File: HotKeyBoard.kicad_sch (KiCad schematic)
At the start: 150 parts, among them J1 Conn_01x12_Socket, J2 Conn_01x12_Socket, SW1 SW_Push, SW10 SW_Push, SW11 SW_Push, SW12 SW_Push, SW13 SW_Push, SW14 SW_Push, SW15 SW_Push, SW16 SW_Push, SW17 SW_Push, SW18 SW_Push, SW19 SW_Push, SW2 SW_Push, SW20 SW_Push, SW21 SW_Push, SW22 SW_Push, SW23 SW_Push, SW24 SW_Push, SW25 SW_Push, SW26 SW_Push, SW27 SW_Push, SW28 SW_Push, SW29 SW_Push, SW3 SW_Push, SW30 SW_Push, SW31 SW_Push, SW32 SW_Push, SW33 SW_Push, SW34 SW_Push, SW35 SW_Push, SW36 SW_Push, SW37 SW_Push, SW38 SW_Push, SW39 SW_Push, SW4 SW_Push, SW40 SW_Push, SW41 SW_Push, SW42 SW_Push, SW43 SW_Push, SW44 SW_Push, SW45 SW_Push, SW46 SW_Push, SW47 SW_Push, SW48 SW_Push, SW49 SW_Push, SW5 SW_Push, SW50 SW_Push, SW51 SW_Push, SW52 SW_Push, SW53 SW_Push, SW54 SW_Push, SW55 SW_Push, SW56 SW_Push, SW57 SW_Push, SW58 SW_Push, SW59 SW_Push, SW6 SW_Push, SW60 SW_Push, SW61 SW_Push, SW62 SW_Push, SW63 SW_Push, SW64 SW_Push, SW65 SW_Push, SW66 SW_Push, SW67 SW_Push, SW68 SW_Push, SW69 SW_Push, SW7 SW_Push, SW70 SW_Push, SW71 SW_Push, SW72 SW_Push, SW8 SW_Push, SW9 SW_Push

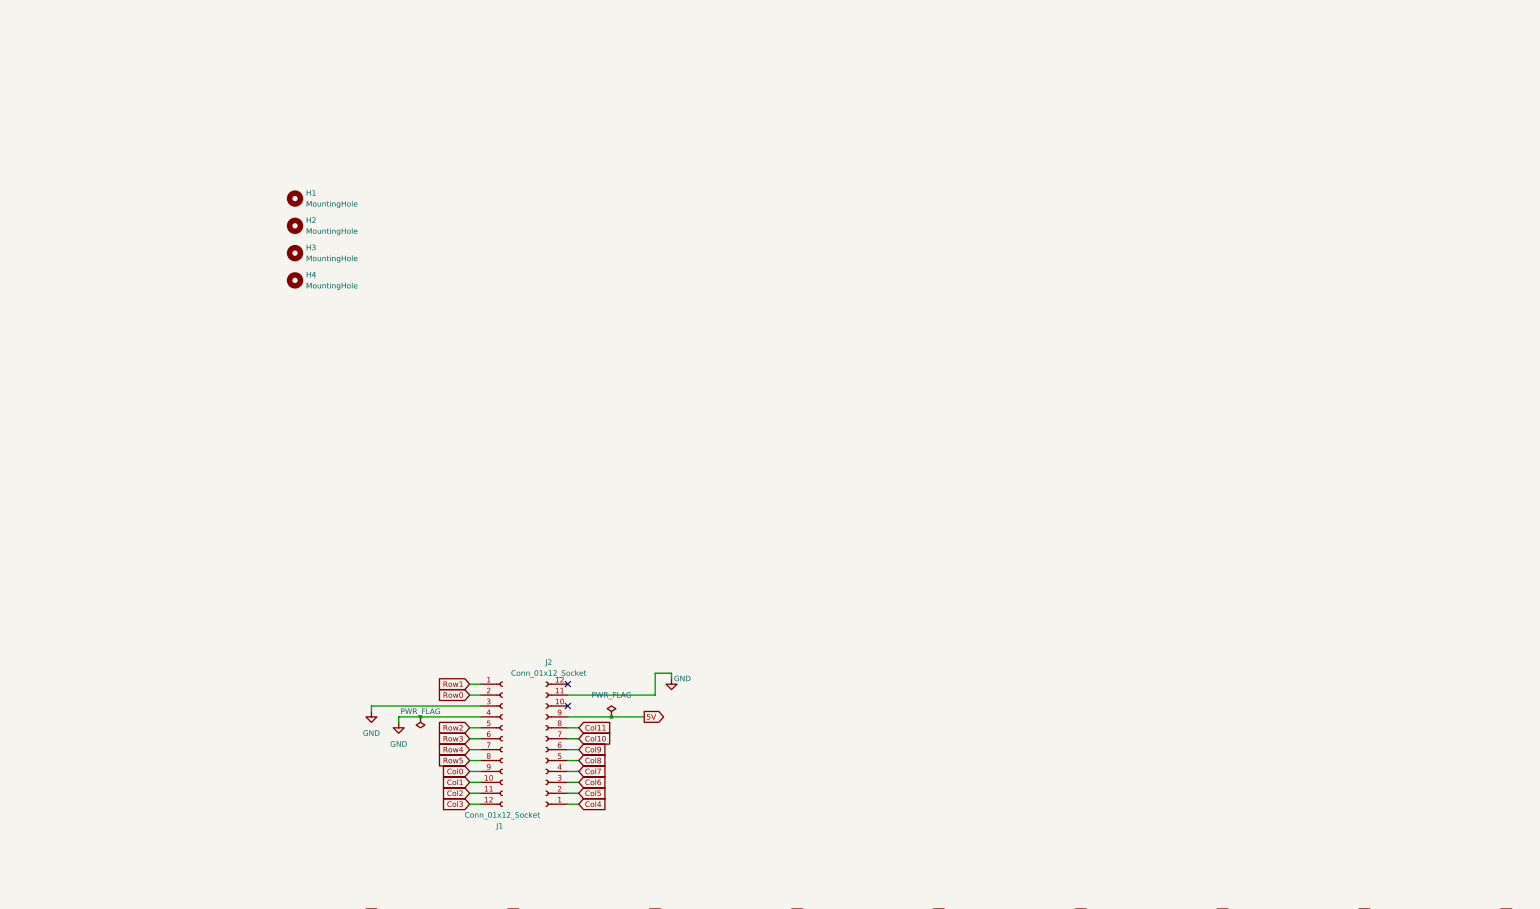
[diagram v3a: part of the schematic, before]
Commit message: Started doing the schematic
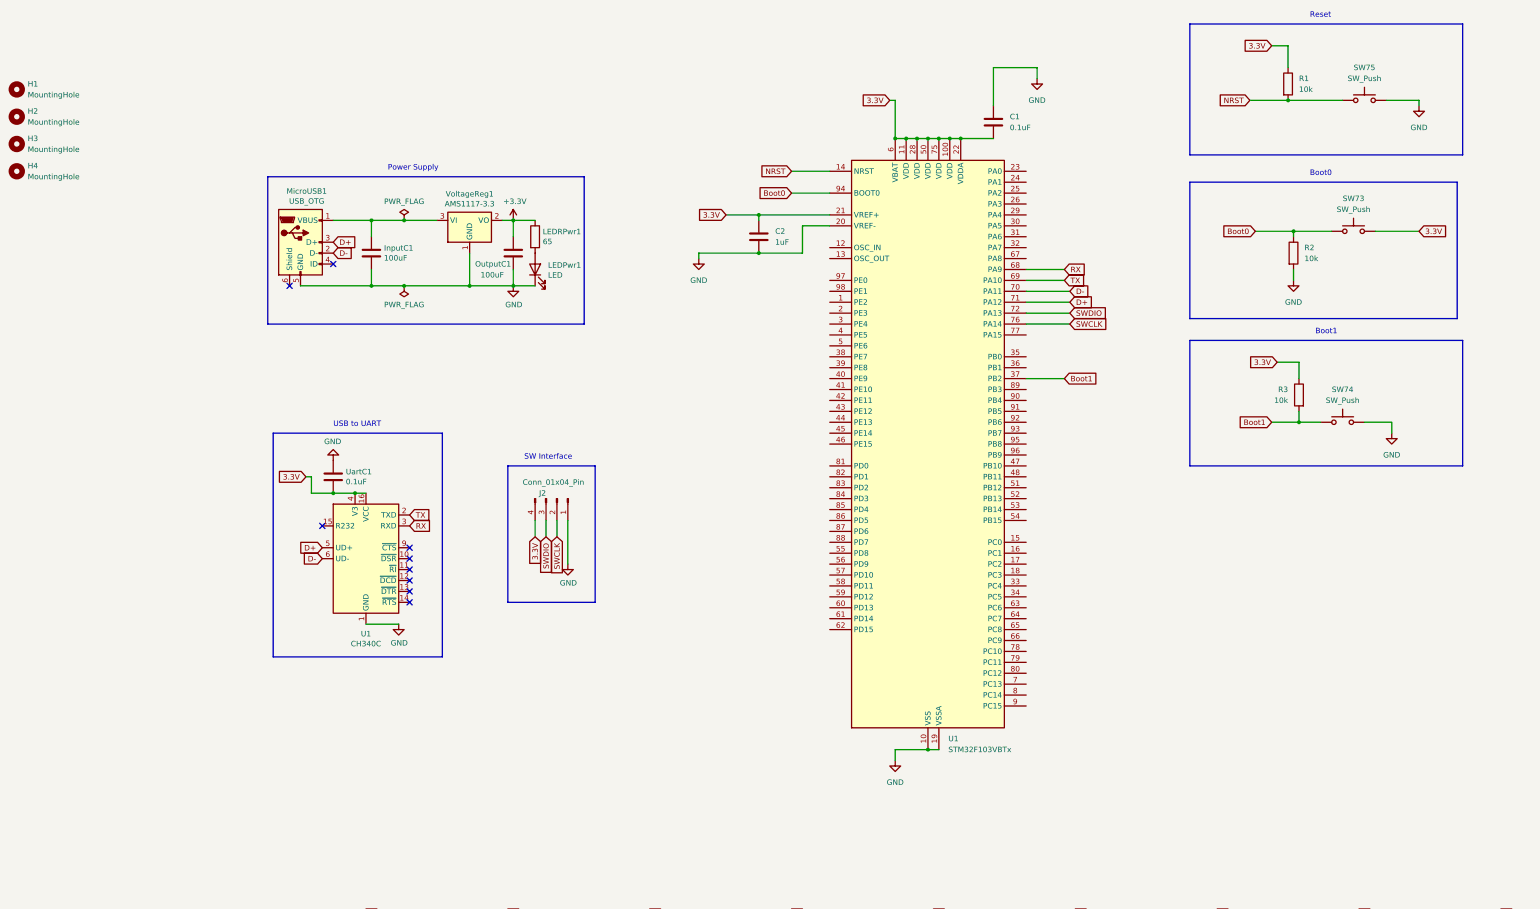
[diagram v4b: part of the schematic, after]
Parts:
- removed J1, J2: Conn_01x12_Socket, Connector_PinHeader_2.54mm:PinHeader_1x12_P2.54mm_Vertical, symbol Connector:Conn_01x12_Socket
- added C1: 0.1uF, symbol Device:C
- added C2: 1uF, symbol Device:C
- added InputC1, OutputC1: 100uF, Capacitor_THT:C_Radial_D5.0mm_H7.0mm_P2.00mm, symbol Device:C
- added J2: Conn_01x04_Pin, symbol Connector:Conn_01x04_Pin
- added LEDPwr1: LED, LED_SMD:LED_0402_1005Metric, symbol Device:LED
- added LEDRPwr1: 65, Resistor_THT:R_Axial_DIN0207_L6.3mm_D2.5mm_P7.62mm_Horizontal, symbol Device:R
- added MicroUSB1: USB_OTG, Connector_USB:USB_Micro-B_Molex_47346-0001, symbol Connector:USB_OTG
- added R1, R2, R3: 10k, symbol Device:R
- added SW73, SW74, SW75: SW_Push, symbol Switch:SW_Push
- added U1: CH340C, Package_SO:SOIC-16_3.9x9.9mm_P1.27mm, symbol Interface_USB:CH340C
- added U1: STM32F103VBTx, Package_QFP:LQFP-100_14x14mm_P0.5mm, symbol MCU_ST_STM32F1:STM32F103VBTx
- added UartC1: 0.1uF, Capacitor_THT:C_Radial_D5.0mm_H7.0mm_P2.00mm, symbol Device:C
- added VoltageReg1: AMS1117-3.3, Package_TO_SOT_SMD:SOT-223-3_TabPin2, symbol Regulator_Linear:AMS1117-3.3
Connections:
- net GND: now also C1.1, C2.2, InputC1.2, J2.1 (Pin_1), LEDPwr1.1 (K), MicroUSB1.5 (GND), OutputC1.2, R2.2, SW74.2, SW75.2, U1.1 (GND), U1.10 (VSS), U1.19 (VSSA), U1.20 (VREF-), U1.27 (VSS), U1.49 (VSS), U1.74 (VSS), U1.99 (VSS), UartC1.1, VoltageReg1.1 (GND)
- new net: LEDPwr1.2 (A), LEDRPwr1.2
- new net: InputC1.1, MicroUSB1.1 (VBUS), VoltageReg1.3 (VI)
- new net +3V3: LEDRPwr1.1, OutputC1.1, VoltageReg1.2 (VO)
- new net 3.3V: C1.2, C2.1, J2.4 (Pin_4), R1.1, R3.1, SW73.2, U1.100 (VDD), U1.11 (VDD), U1.16 (VCC), U1.21 (VREF+), U1.22 (VDDA), U1.28 (VDD), U1.4 (V3), U1.50 (VDD), U1.6 (VBAT), U1.75 (VDD), UartC1.2
- new net Boot0: R2.1, SW73.1, U1.94 (BOOT0)
- new net Boot1: R3.2, SW74.1, U1.37 (PB2)
- new net D+: MicroUSB1.3 (D+), U1.5 (UD+), U1.71 (PA12)
- new net D-: MicroUSB1.2 (D-), U1.6 (UD-), U1.70 (PA11)
- new net NRST: R1.2, SW75.1, U1.14 (NRST)
- new net RX: U1.3 (RXD), U1.68 (PA9)
- new net SWCLK: J2.2 (Pin_2), U1.76 (PA14)
- new net SWDIO: J2.3 (Pin_3), U1.72 (PA13)
- new net TX: U1.2 (TXD), U1.69 (PA10)
- no-connect marks 2 -> 9
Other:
- note added: "Boot0"
- note added: "Boot1"
- note added: "Power Supply"
- note added: "Reset"
- note added: "SW Interface"
- note added: "USB to UART"
- moved on the sheet: H1, H2, H3, H4

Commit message: Finished schematic
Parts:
- added D100, D101, D102, D103, D104, D105, D106, D107, D108, D109, D110, D111, D112, D113, D114, D115, D116, D117, D118, D119, D120, D121, D122, D123, D124, D125, D126, D127, D128, D129, D130, D131, D132, D133, D134, D135, D136, D137, D138, D139, D140, D141, D142, D143, D144, D145, D146, D147, D148, D149, D150, D151, D152, D153, D154, D155, D156, D157, D158, D159, D160, D161, D162, D163, D164, D165, D166, D167, D168, D169, D170, D171, D172, D173, D174, D175, D176, D177, D178, D179, D180, D181, D182, D183, D184, D185, D186, D187, D188, D189, D190, D191, D192, D97, D98, D99: LED, LED_SMD:LED_0402_1005Metric, symbol Device:LED
- added D73, D74, D75, D76, D77, D78, D79, D80, D81, D82, D83, D84, D85, D86, D87, D88, D89, D90, D91, D92, D93, D94, D95, D96: D, Diode_SMD:D_SOD-323, symbol Device:D
- added J1: Conn_01x04_Pin, Connector_PinHeader_2.54mm:PinHeader_1x04_P2.54mm_Vertical, symbol Connector:Conn_01x04_Pin
- added J3: USB_VOLTAGE Measuring Point, Connector_PinHeader_2.54mm:PinHeader_1x01_P2.54mm_Vertical, symbol Connector:Conn_01x01_Pin
- added J4: LED_VOLTAGE Measuring Point 1, Connector_PinHeader_2.54mm:PinHeader_1x01_P2.54mm_Vertical, symbol Connector:Conn_01x01_Pin
- added J5: LED_VOLTAGE Measuring Point 2, Connector_PinHeader_2.54mm:PinHeader_1x01_P2.54mm_Vertical, symbol Connector:Conn_01x01_Pin
- added Q1, Q2, Q3, Q4, Q5, Q6: IRLZ34N, Package_TO_SOT_THT:TO-220-3_Vertical, symbol Transistor_FET:IRLZ34N
- added R10, R11, R12, R13, R14, R15, R16, R17, R18, R19, R20, R21, R22, R23, R24, R25, R26, R27, R28, R29, R30, R31, R32, R33, R34, R35, R36, R37, R38, R39, R4, R40, R41, R42, R43, R44, R45, R46, R47, R48, R49, R5, R50, R51, R52, R53, R54, R55, R56, R57, R58, R59, R6, R60, R61, R62, R63, R64, R65, R66, R67, R68, R69, R7, R70, R71, R72, R73, R74, R75, R76, R77, R78, R79, R8, R80, R81, R82, R83, R84, R85, R86, R87, R88, R89, R9, R90, R91, R92, R93, R94, R95, R96, R97, R98, R99: R, Resistor_SMD:R_0603_1608Metric, symbol Device:R
- added SW76, SW77, SW78, SW80, SW81, SW82, SW83, SW84, SW86, SW87, SW88, SW89, SW90, SW92, SW93, SW94, SW95, SW96, SW98, SW99: SW_Push, Button_Switch_Keyboard:SW_Cherry_MX_1.00u_PCB, symbol Switch:SW_Push
- added SW79, SW85, SW91, SW97: SW_Push, Button_Switch_Keyboard:SW_Cherry_MX_1.75u_PCB, symbol Switch:SW_Push
- added U2, U4: AMS1117-3.3, Package_TO_SOT_SMD:SOT-223-3_TabPin2, symbol Regulator_Linear:AMS1117-3.3
- C1: footprint (none) -> Capacitor_SMD:C_0402_1005Metric; LCSC (none) -> C307331
- C2: footprint (none) -> Capacitor_SMD:C_0603_1608Metric; LCSC (none) -> C15849
- InputC1, OutputC1: footprint Capacitor_THT:C_Radial_D5.0mm_H7.0mm_P2.00mm -> Capacitor_SMD:C_1206_3216Metric; LCSC (none) -> C15008
- J2: footprint (none) -> Connector_PinHeader_2.54mm:PinHeader_1x04_P2.54mm_Vertical
- LEDPwr1: LCSC (none) -> C71911
- LEDRPwr1: LCSC (none) -> C307279
- R1, R2, R3: footprint (none) -> Resistor_SMD:R_0603_1608Metric; LCSC (none) -> C25804
- SW73, SW74, SW75: footprint (none) -> Button_Switch_Keyboard:SW_Cherry_MX_1.00u_PCB
- U1: LCSC (none) -> C84681
- UartC1: footprint Capacitor_THT:C_Radial_D5.0mm_H7.0mm_P2.00mm -> Capacitor_SMD:C_0402_1005Metric; LCSC (none) -> C307331
- VoltageReg1: LCSC (none) -> C347256
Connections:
- net +3V3 is gone; now on net 3.3V: LEDRPwr1.1, OutputC1.1, VoltageReg1.2 (VO)
- net 3.3V: now also J1.4 (Pin_4)
- net Col0: now also U1.81 (PD0)
- net Col1: now also U1.82 (PD1)
- net Col10: now also U1.57 (PD10)
- net Col11: now also U1.58 (PD11)
- net Col2: now also U1.83 (PD2)
- net Col3: now also U1.84 (PD3)
- net Col4: now also U1.85 (PD4)
- net Col5: now also U1.86 (PD5)
- net Col6: now also U1.87 (PD6)
- net Col7: now also U1.88 (PD7)
- net Col8: now also U1.55 (PD8)
- net Col9: now also U1.56 (PD9)
- net GND: now also J1.3 (Pin_3), Q1.3 (S), Q2.3 (S), Q3.3 (S), Q4.3 (S), Q5.3 (S), Q6.3 (S), U2.1 (GND), U4.1 (GND)
- net Row0: now also U1.97 (PE0), D73.1 (K), D79.1 (K), D85.1 (K), D91.1 (K)
- net Row1: now also U1.98 (PE1), D74.1 (K), D80.1 (K), D86.1 (K), D92.1 (K)
- net Row2: now also U1.1 (PE2), D75.1 (K), D81.1 (K), D87.1 (K), D93.1 (K)
- net Row3: now also U1.2 (PE3), D76.1 (K), D82.1 (K), D88.1 (K), D94.1 (K)
- net Row4: now also U1.3 (PE4), D77.1 (K), D83.1 (K), D89.1 (K), D95.1 (K)
- net Row5: now also U1.4 (PE5), D78.1 (K), D84.1 (K), D90.1 (K), D96.1 (K)
- net USB_VOLT: now reaches InputC1.1, MicroUSB1.1 (VBUS), VoltageReg1.3 (VI)
- net USB_VOLT: now also J3.1 (Pin_1), U2.3 (VI), U4.3 (VI)
- net Row7: now reaches U1.38 (PE7)
- net Row8: now reaches U1.39 (PE8)
- net Row9: now reaches U1.40 (PE9)
- net Row10: now reaches U1.41 (PE10)
- net Row11: now reaches U1.42 (PE11)
- net Row12: now reaches U1.43 (PE12)
- net Row13: now reaches U1.44 (PE13)
- net Row14: now reaches U1.45 (PE14)
- net Row15: now reaches U1.46 (PE15)
- net I2C_SCL: now reaches U1.47 (PB10)
- net I2C_SCL: now also J1.2 (Pin_2)
- net I2C_SDA: now reaches U1.48 (PB11)
- net I2C_SDA: now also J1.1 (Pin_1)
- net Row6: now reaches U1.5 (PE6)
- net Col12: now reaches U1.59 (PD12)
- net Col12: now also SW76.1, SW77.1, SW78.1, SW79.1, SW80.1, SW81.1
- net Col13: now reaches U1.60 (PD13)
- net Col13: now also SW82.1, SW83.1, SW84.1, SW85.1, SW86.1, SW87.1
- net Col14: now reaches U1.61 (PD14)
- net Col14: now also SW88.1, SW89.1, SW90.1, SW91.1, SW92.1, SW93.1
- net Col15: now reaches U1.62 (PD15)
- net Col15: now also SW94.1, SW95.1, SW96.1, SW97.1, SW98.1, SW99.1
- net Gate3: now reaches U1.63 (PC6)
- net Gate3: now also Q4.1 (G)
- net Gate4: now reaches U1.64 (PC7)
- net Gate4: now also Q5.1 (G)
- net Gate5: now reaches U1.65 (PC8)
- net Gate5: now also Q6.1 (G)
- net Gate0: now reaches U1.89 (PB3)
- net Gate0: now also Q1.1 (G)
- net Gate1: now reaches U1.90 (PB4)
- net Gate1: now also Q2.1 (G)
- net Gate2: now reaches U1.91 (PB5)
- net Gate2: now also Q3.1 (G)
- new net: D145.2 (A), R52.2
- new net: D186.2 (A), R93.2
- new net: D101.2 (A), R8.2
- new net: D85.2 (A), SW88.2
- new net: D86.2 (A), SW89.2
- new net: D137.2 (A), R44.2
- new net: D108.2 (A), R15.2
- new net: D183.2 (A), R90.2
- new net: D180.2 (A), R87.2
- new net: D128.2 (A), R35.2
- new net: D94.2 (A), SW97.2
- new net: D187.2 (A), R94.2
- new net: D170.2 (A), R77.2
- new net: D158.2 (A), R65.2
- new net: D107.2 (A), R14.2
- new net: D126.2 (A), R33.2
- new net: D160.2 (A), R67.2
- new net: D73.2 (A), SW76.2
- new net: D189.2 (A), R96.2
- new net: D165.2 (A), R72.2
- new net: D157.2 (A), R64.2
- new net: D115.2 (A), R22.2
- new net: D83.2 (A), SW86.2
- new net: D92.2 (A), SW95.2
- new net: D182.2 (A), R89.2
- new net: D106.2 (A), R13.2
- new net: D149.2 (A), R56.2
- new net: D184.2 (A), R91.2
- new net: D134.2 (A), R41.2
- new net: D143.2 (A), R50.2
- new net: D179.2 (A), R86.2
- new net: D111.2 (A), R18.2
- new net: D123.2 (A), R30.2
- new net: D129.2 (A), R36.2
- new net: D150.2 (A), R57.2
- new net: D113.2 (A), R20.2
- new net: D120.2 (A), R27.2
- new net: D118.2 (A), R25.2
- new net: D135.2 (A), R42.2
- new net: D77.2 (A), SW80.2
- new net: D140.2 (A), R47.2
- new net: D81.2 (A), SW84.2
- new net: D164.2 (A), R71.2
- new net: D174.2 (A), R81.2
- new net: D103.2 (A), R10.2
- new net: D130.2 (A), R37.2
- new net: D117.2 (A), R24.2
- new net: D192.2 (A), R99.2
- new net: D102.2 (A), R9.2
- new net: D80.2 (A), SW83.2
- new net: D138.2 (A), R45.2
- new net: D88.2 (A), SW91.2
- new net: D124.2 (A), R31.2
- new net: D104.2 (A), R11.2
- new net: D171.2 (A), R78.2
- new net: D141.2 (A), R48.2
- new net: D177.2 (A), R84.2
- new net: D121.2 (A), R28.2
- new net: D168.2 (A), R75.2
- new net: D125.2 (A), R32.2
- new net: D97.2 (A), R4.2
- new net: D105.2 (A), R12.2
- new net: D109.2 (A), R16.2
- new net: D176.2 (A), R83.2
- new net: D175.2 (A), R82.2
- new net: D156.2 (A), R63.2
- new net: D185.2 (A), R92.2
- new net: D169.2 (A), R76.2
- new net: D127.2 (A), R34.2
- new net: D91.2 (A), SW94.2
- new net: D100.2 (A), R7.2
- new net: D139.2 (A), R46.2
- new net: D74.2 (A), SW77.2
- new net: D131.2 (A), R38.2
- new net: D95.2 (A), SW98.2
- new net: D167.2 (A), R74.2
- new net: D112.2 (A), R19.2
- new net: D162.2 (A), R69.2
- new net: D122.2 (A), R29.2
- new net: D144.2 (A), R51.2
- new net: D142.2 (A), R49.2
- new net: D87.2 (A), SW90.2
- new net: D133.2 (A), R40.2
- new net: D76.2 (A), SW79.2
- new net: D93.2 (A), SW96.2
- new net: D173.2 (A), R80.2
- new net: D89.2 (A), SW92.2
- new net: D99.2 (A), R6.2
- new net: D132.2 (A), R39.2
- new net: D110.2 (A), R17.2
- new net: D159.2 (A), R66.2
- new net: D163.2 (A), R70.2
- new net: D191.2 (A), R98.2
- new net: D178.2 (A), R85.2
- new net: D190.2 (A), R97.2
- new net: D161.2 (A), R68.2
- new net: D136.2 (A), R43.2
- new net: D155.2 (A), R62.2
- new net: D148.2 (A), R55.2
- new net: D172.2 (A), R79.2
- new net: D79.2 (A), SW82.2
- new net: D147.2 (A), R54.2
- new net: D78.2 (A), SW81.2
- new net: D114.2 (A), R21.2
- new net: D75.2 (A), SW78.2
- new net: D153.2 (A), R60.2
- new net: D181.2 (A), R88.2
- new net: D152.2 (A), R59.2
- new net: D116.2 (A), R23.2
- new net: D96.2 (A), SW99.2
- new net: D90.2 (A), SW93.2
- new net: D98.2 (A), R5.2
- new net: D188.2 (A), R95.2
- new net: D84.2 (A), SW87.2
- new net: D166.2 (A), R73.2
- new net: D151.2 (A), R58.2
- new net: D154.2 (A), R61.2
- new net: D146.2 (A), R53.2
- new net: D82.2 (A), SW85.2
- new net: D119.2 (A), R26.2
- new net LED_INPUT_VOLTAGE1: J4.1 (Pin_1), R10.1, R11.1, R12.1, R13.1, R14.1, R15.1, R16.1, R17.1, R18.1, R19.1, R20.1, R21.1, R22.1, R23.1, R24.1, R25.1, R26.1, R27.1, R28.1, R29.1, R30.1, R31.1, R32.1, R33.1, R34.1, R35.1, R36.1, R37.1, R38.1, R39.1, R4.1, R40.1, R41.1, R42.1, R43.1, R44.1, R45.1, R46.1, R47.1, R48.1, R49.1, R5.1, R50.1, R51.1, R6.1, R7.1, R8.1, R9.1, U2.2 (VO)
- new net LED_INPUT_VOLTAGE2: J5.1 (Pin_1), R52.1, R53.1, R54.1, R55.1, R56.1, R57.1, R58.1, R59.1, R60.1, R61.1, R62.1, R63.1, R64.1, R65.1, R66.1, R67.1, R68.1, R69.1, R70.1, R71.1, R72.1, R73.1, R74.1, R75.1, R76.1, R77.1, R78.1, R79.1, R80.1, R81.1, R82.1, R83.1, R84.1, R85.1, R86.1, R87.1, R88.1, R89.1, R90.1, R91.1, R92.1, R93.1, R94.1, R95.1, R96.1, R97.1, R98.1, R99.1, U4.2 (VO)
- new net Mosfet0: D100.1 (K), D101.1 (K), D102.1 (K), D103.1 (K), D104.1 (K), D105.1 (K), D106.1 (K), D107.1 (K), D108.1 (K), D109.1 (K), D110.1 (K), D111.1 (K), D112.1 (K), D97.1 (K), D98.1 (K), D99.1 (K), Q1.2 (D)
- new net Mosfet1: D113.1 (K), D114.1 (K), D115.1 (K), D116.1 (K), D117.1 (K), D118.1 (K), D119.1 (K), D120.1 (K), D121.1 (K), D122.1 (K), D123.1 (K), D124.1 (K), D125.1 (K), D126.1 (K), D127.1 (K), D128.1 (K), Q2.2 (D)
- new net Mosfet2: D129.1 (K), D130.1 (K), D131.1 (K), D132.1 (K), D133.1 (K), D134.1 (K), D135.1 (K), D136.1 (K), D137.1 (K), D138.1 (K), D139.1 (K), D140.1 (K), D141.1 (K), D142.1 (K), D143.1 (K), D144.1 (K), Q3.2 (D)
- new net Mosfet3: D145.1 (K), D146.1 (K), D147.1 (K), D148.1 (K), D149.1 (K), D150.1 (K), D151.1 (K), D152.1 (K), D153.1 (K), D154.1 (K), D155.1 (K), D156.1 (K), D157.1 (K), D158.1 (K), D159.1 (K), D160.1 (K), Q4.2 (D)
- new net Mosfet4: D161.1 (K), D162.1 (K), D163.1 (K), D164.1 (K), D165.1 (K), D166.1 (K), D167.1 (K), D168.1 (K), D169.1 (K), D170.1 (K), D171.1 (K), D172.1 (K), D173.1 (K), D174.1 (K), D175.1 (K), D176.1 (K), Q5.2 (D)
- new net Mosfet5: D177.1 (K), D178.1 (K), D179.1 (K), D180.1 (K), D181.1 (K), D182.1 (K), D183.1 (K), D184.1 (K), D185.1 (K), D186.1 (K), D187.1 (K), D188.1 (K), D189.1 (K), D190.1 (K), D191.1 (K), D192.1 (K), Q6.2 (D)
- no-connect marks 9 -> 44
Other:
- note added: "LED Power Supply"
- note added: "LED Stripe control"
- note added: "OLED Display"
- moved on the sheet: D1, D10, D11, D12, D13, D14, D15, D16, D17, D18, D19, D2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

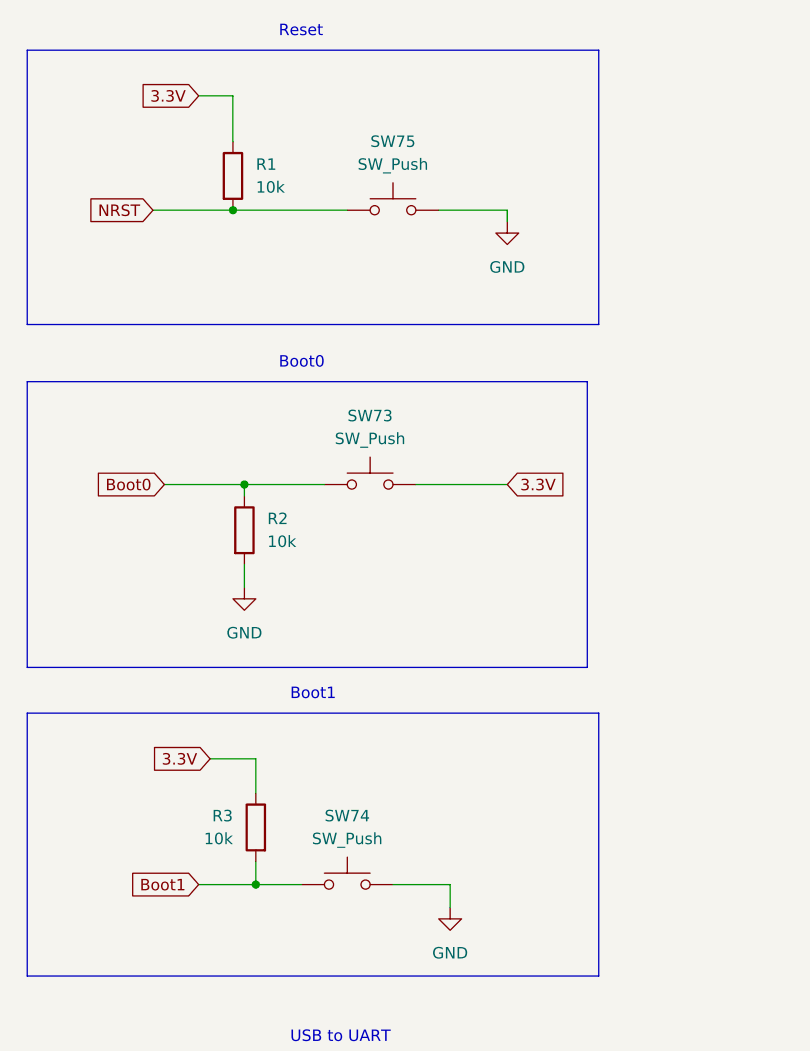
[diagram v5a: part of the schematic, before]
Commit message: Started layout
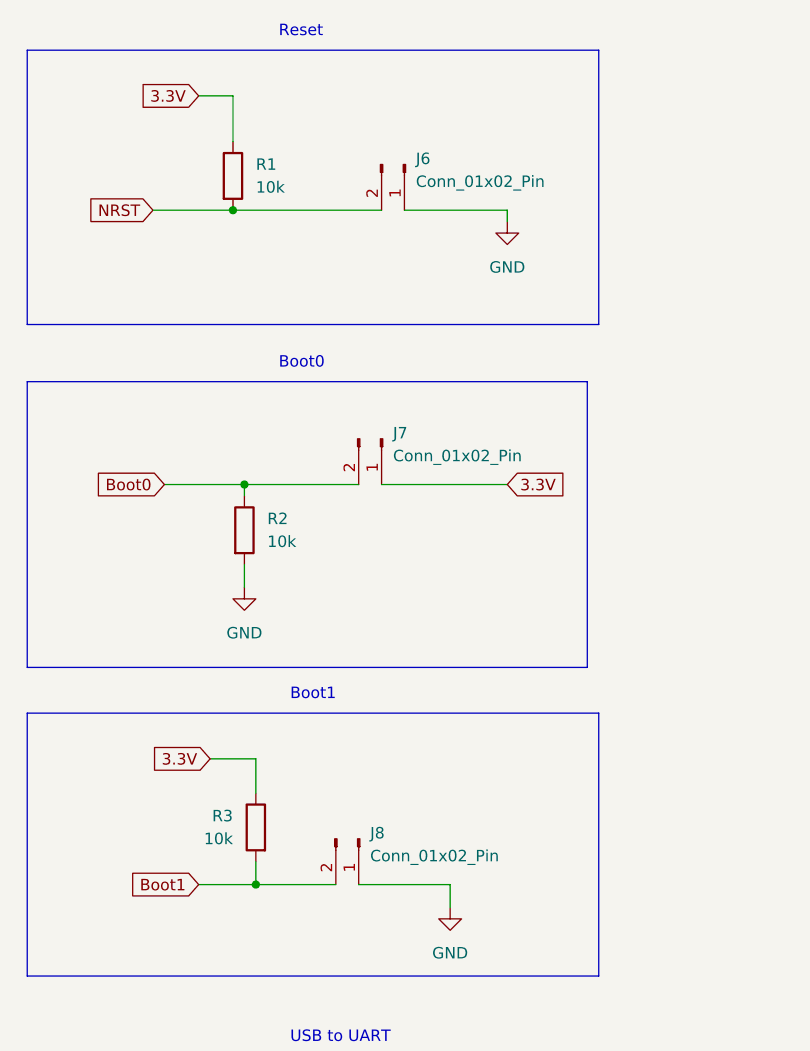
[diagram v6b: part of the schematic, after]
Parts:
- removed SW73, SW74, SW75: SW_Push, Button_Switch_Keyboard:SW_Cherry_MX_1.00u_PCB, symbol Switch:SW_Push
- added J6, J7, J8: Conn_01x02_Pin, Connector_PinHeader_2.54mm:PinHeader_1x02_P2.54mm_Vertical, symbol Connector:Conn_01x02_Pin
- LEDRPwr1: footprint Resistor_THT:R_Axial_DIN0207_L6.3mm_D2.5mm_P7.62mm_Horizontal -> Resistor_SMD:R_0201_0603Metric
- Q1, Q2, Q3, Q4, Q5, Q6: footprint Package_TO_SOT_THT:TO-220-3_Vertical -> Package_TO_SOT_SMD:TO-263-2
- SW11, SW17: footprint Button_Switch_Keyboard:SW_Cherry_MX_1.25u_PCB -> Button_Switch_Keyboard:SW_Cherry_MX_1.00u_PCB
- SW12: footprint Button_Switch_Keyboard:SW_Cherry_MX_2.00u_PCB -> Button_Switch_Keyboard:SW_Cherry_MX_1.25u_PCB
- SW18, SW6: footprint Button_Switch_Keyboard:SW_Cherry_MX_1.00u_PCB -> Button_Switch_Keyboard:SW_Cherry_MX_1.25u_PCB
- SW2: footprint Button_Switch_Keyboard:SW_Cherry_MX_1.50u_PCB -> Button_Switch_Keyboard:SW_Cherry_MX_1.00u_PCB
- SW23: footprint Button_Switch_Keyboard:SW_Cherry_MX_2.25u_PCB -> Button_Switch_Keyboard:SW_Cherry_MX_1.00u_PCB
- SW24: footprint Button_Switch_Keyboard:SW_Cherry_MX_1.50u_PCB -> Button_Switch_Keyboard:SW_Cherry_MX_6.25u_PCB
- SW3: footprint Button_Switch_Keyboard:SW_Cherry_MX_1.75u_PCB -> Button_Switch_Keyboard:SW_Cherry_MX_1.50u_PCB
- SW35: footprint Button_Switch_Keyboard:SW_Cherry_MX_6.25u_PCB -> Button_Switch_Keyboard:SW_Cherry_MX_1.00u_PCB
- SW4: footprint Button_Switch_Keyboard:SW_Cherry_MX_2.25u_PCB -> Button_Switch_Keyboard:SW_Cherry_MX_1.75u_PCB
- SW5: footprint Button_Switch_Keyboard:SW_Cherry_MX_1.25u_PCB -> Button_Switch_Keyboard:SW_Cherry_MX_2.25u_PCB
- SW70, SW85: footprint Button_Switch_Keyboard:SW_Cherry_MX_1.75u_PCB -> Button_Switch_Keyboard:SW_Cherry_MX_1.00u_PCB
- SW71: footprint Button_Switch_Keyboard:SW_Cherry_MX_1.00u_PCB -> Button_Switch_Keyboard:SW_Cherry_MX_1.75u_PCB
- SW79: footprint Button_Switch_Keyboard:SW_Cherry_MX_1.75u_PCB -> Button_Switch_Keyboard:SW_Cherry_MX_2.25u_PCB
- SW83: footprint Button_Switch_Keyboard:SW_Cherry_MX_1.00u_PCB -> Button_Switch_Keyboard:SW_Cherry_MX_2.00u_PCB
- SW84: footprint Button_Switch_Keyboard:SW_Cherry_MX_1.00u_PCB -> Button_Switch_Keyboard:SW_Cherry_MX_1.50u_PCB
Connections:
- net 3.3V: now also J7.1 (Pin_1)
- net Boot0: now also J7.2 (Pin_2)
- net Boot1: now also J8.2 (Pin_2)
- net GND: now also J6.1 (Pin_1), J8.1 (Pin_1)
- net NRST: now also J6.2 (Pin_2)

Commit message: Continued layout, deleted firmware
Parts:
- SW5: footprint Button_Switch_Keyboard:SW_Cherry_MX_2.25u_PCB -> Button_Switch_Keyboard:SW_Cherry_MX_1.25u_PCB
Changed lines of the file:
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@@
       (effects (font (size 1.27 1.27)))
     )
-    (property "Footprint" "Button_Switch_Keyboard:SW_Cherry_MX_2.25u_PCB" (at 62.23 313.69 0)
+    (property "Footprint" "Button_Switch_Keyboard:SW_Cherry_MX_1.25u_PCB" (at 62.23 313.69 0)
       (effects (font (size 1.27 1.27)) hide)
     )

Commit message: Finished single sided layout
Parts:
- removed J6, J7, J8: Conn_01x02_Pin, Connector_PinHeader_2.54mm:PinHeader_1x02_P2.54mm_Vertical, symbol Connector:Conn_01x02_Pin
- removed U1: CH340C, Package_SO:SOIC-16_3.9x9.9mm_P1.27mm, symbol Interface_USB:CH340C
- removed UartC1: 0.1uF, Capacitor_SMD:C_0402_1005Metric, symbol Device:C
- added R100: 1.5k, Resistor_SMD:R_0603_1608Metric, symbol Device:R
- LEDRPwr1: footprint Resistor_SMD:R_0201_0603Metric -> Resistor_SMD:R_0603_1608Metric
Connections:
- net 3.3V: now also R100.1
- net D+: now also R100.2
- no-connect marks 44 -> 37
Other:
- note removed: "USB to UART"
